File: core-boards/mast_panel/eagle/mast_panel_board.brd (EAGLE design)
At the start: 63.5 x 47.9 mm, 30 parts, among them J1 2-PIN_2MM-V, J4 4-PIN_2MM-H, U1 ATMEGA328P-AUR, U3 MCP2551T-I/SN

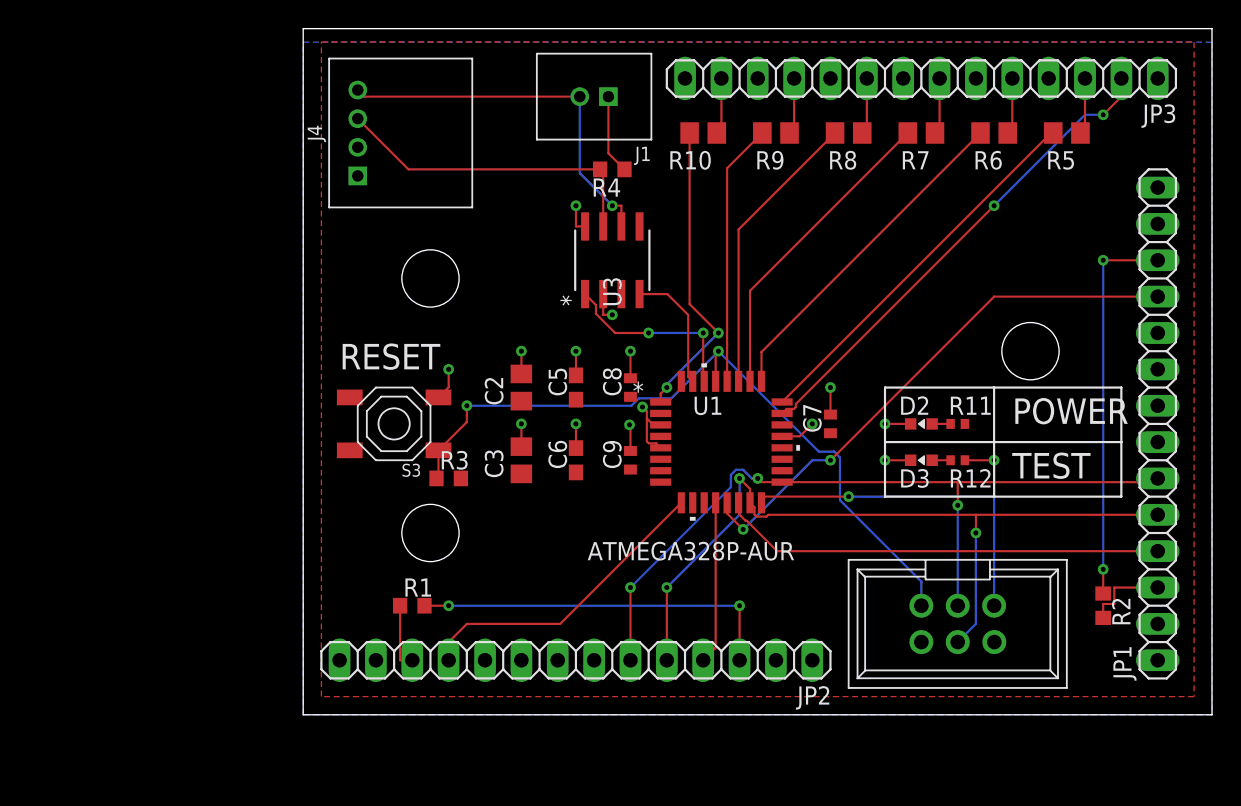
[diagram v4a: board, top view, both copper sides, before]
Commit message: CAN Addition
Added the new CAN Controller. Routing on the board still needs to be done.
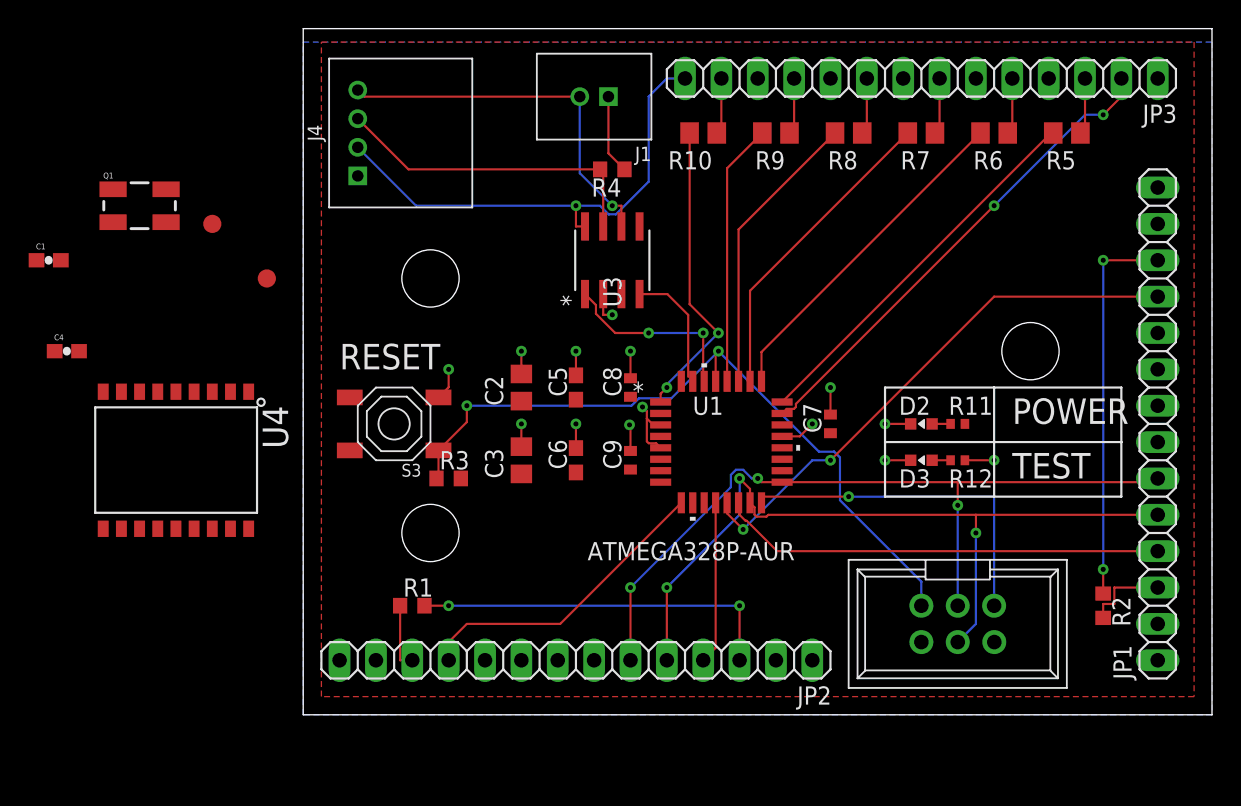
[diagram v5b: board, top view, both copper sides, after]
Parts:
- added C1, C4: 22pF, SparkFun-Capacitors:0603-CAP
- added Q1: 16MHz, SparkFun-FreqCtrl:CRYSTAL-SMD-5X3
- added TP1, TP2: TEST-POINT3X5, SparkFun-Passives:PAD.03X.05
- added U4: MCP2515, SparkFun-DigitalIC:SO-18W
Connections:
- new net CAN_SS: U1.31, U4.16
- new net MBED_CAN_INT: U1.32, U4.12
- new net N$17: C4.2, Q1.3, U4.8
- new net N$18: C1.2, Q1.1, U4.7
- new net VDD: U4.18
- new net VSS: U4.9
- net GND: now also C1.1, C4.1
- net LCD_MOSI: now also U4.14
- net LCD_SCLK: now also U4.13
- net MBED_CAN_RD: now also TP2.P$1, U4.1; no longer U1.30
- net MBED_CAN_TD: now also TP1.P$1, U4.2; no longer U1.31
- net RESET: now also U4.17
- net TEST_LED: now also U4.15
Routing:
- net GND: track 29.5 -> 61.7 mm
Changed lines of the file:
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@@
 <drawing>
 <settings>
-<setting alwaysvectorfont="yes"/>
+<setting alwaysvectorfont="no"/>
 <setting verticaltext="up"/>
 </settings>
@@
 <attribute name="VALUE" x="51.435" y="48.26" size="1.27" layer="27" rot="R180"/>
 </element>
+<element name="U4" library="SparkFun-DigitalIC" package="SO-18W" value="MCP2515" x="13.97" y="22.86" smashed="yes" rot="R180">
+<attribute name="NAME" x="20.0279" y="26.67" size="1.778" layer="25" ratio="10" rot="R270"/>
+<attribute name="PROD_ID" value="IC-09906" x="13.97" y="21.59" size="1.778" layer="27" rot="R180" display="off"/>
+<attribute name="VALUE" x="6.0579" y="26.67" size="1.778" layer="27" ratio="10" rot="R270"/>
+</element>
+<element name="Q1" library="SparkFun-FreqCtrl" package="CRYSTAL-SMD-5X3" value="16MHz" x="11.43" y="40.64" smashed="yes">
+<attribute name="NAME" x="8.89" y="42.545" size="0.4064" layer="25"/>
+<attribute name="PROD_ID" value="XTAL-08218" x="11.43" y="41.91" size="1.778" layer="27" display="off"/>
+<attribute name="VALUE" x="8.89" y="38.1" size="0.4064" layer="27"/>
+</element>
+<element name="C1" library="SparkFun-Capacitors" package="0603-CAP" value="22pF" x="5.08" y="36.83" smashed="yes">
+<attribute name="NAME" x="4.191" y="37.592" size="0.4064" layer="25" font="vector"/>
+<attribute name="PROD_ID" value="CAP-07876" x="-2.54" y="31.75" size="1.778" layer="27" display="off"/>
+<attribute name="VALUE" x="4.064" y="35.687" size="0.4064" layer="27" font="vector"/>
+</element>
+<element name="C4" library="SparkFun-Capacitors" package="0603-CAP" value="22pF" x="6.35" y="30.48" smashed="yes">
+<attribute name="NAME" x="5.461" y="31.242" size="0.4064" layer="25" font="vector"/>
+<attribute name="PROD_ID" value="CAP-07876" x="-5.08" y="21.59" size="1.778" layer="27" display="off"/>
+<attribute name="VALUE" x="5.334" y="29.337" size="0.4064" layer="27" font="vector"/>
+</element>
+<element name="TP1" library="SparkFun-Passives" package="PAD.03X.05" value="TEST-POINT3X5" x="16.51" y="39.37" smashed="yes"/>
+<element name="TP2" library="SparkFun-Passives" package="PAD.03X.05" value="TEST-POINT3X5" x="20.32" y="35.56" smashed="yes"/>
 </elements>
 <signals>
@@
 <wire x1="33.02" y1="27.96" x2="33.02" y2="29.21" width="0.1524" layer="1"/>
 <via x="33.02" y="29.21" extent="1-16" drill="0.35"/>
+<contactref element="C4" pad="1"/>
+<contactref element="C1" pad="1"/>
+<wire x1="26.67" y1="44.72" x2="30.75" y2="40.64" width="0.1524" layer="16"/>
+<wire x1="30.75" y1="40.64" x2="41.91" y2="40.64" width="0.1524" layer="16"/>
+<wire x1="44.19865" y1="40.0332" x2="44.70135" y2="40.0332" width="0.1524" layer="16"/>
+<wire x1="41.91" y1="40.64" x2="43.59185" y2="40.64" width="0.1524" layer="16"/>
+<wire x1="43.59185" y1="40.64" x2="44.19865" y2="40.0332" width="0.1524" layer="16"/>
+<wire x1="44.70135" y1="40.0332" x2="46.99" y2="42.32185" width="0.1524" layer="16"/>
+<wire x1="46.99" y1="42.32185" x2="46.99" y2="48.26" width="0.1524" layer="16"/>
+<wire x1="46.99" y1="48.26" x2="48.26" y2="49.53" width="0.1524" layer="16"/>
+<wire x1="48.26" y1="49.53" x2="49.53" y2="49.53" width="0.1524" layer="16"/>
+<wire x1="74.93" y1="49.53" x2="82.55" y2="41.91" width="0" layer="19" extent="1-1"/>
+<wire x1="69.85" y1="49.53" x2="74.93" y2="49.53" width="0" layer="19" extent="1-1"/>
+<wire x1="64.77" y1="49.53" x2="69.85" y2="49.53" width="0" layer="19" extent="1-1"/>
+<wire x1="59.69" y1="49.53" x2="64.77" y2="49.53" width="0" layer="19" extent="1-1"/>
+<wire x1="54.61" y1="49.53" x2="59.69" y2="49.53" width="0" layer="19" extent="1-1"/>
+<wire x1="49.53" y1="49.53" x2="54.61" y2="49.53" width="0" layer="19" extent="1-1"/>
+<wire x1="43.815" y1="34.4678" x2="42.545" y2="39.1922" width="0" layer="19" extent="1-1"/>
+<wire x1="45.72" y1="30.48" x2="44.45" y2="33.02" width="0" layer="19" extent="1-1"/>
+<wire x1="46.561" y1="26.58061875" x2="45.72" y2="28.59" width="0" layer="19" extent="1-1"/>
+<wire x1="45.65308125" y1="25.33308125" x2="46.561" y2="26.58061875" width="0" layer="19" extent="1-1"/>
+<wire x1="41.91" y1="30.48" x2="44.45" y2="33.02" width="0" layer="19" extent="1-1"/>
+<wire x1="41.91" y1="25.4" x2="41.91" y2="28.79" width="0" layer="19" extent="1-1"/>
+<wire x1="38.1" y1="30.48" x2="41.91" y2="30.48" width="0" layer="19" extent="1-1"/>
+<wire x1="38.1" y1="25.4" x2="38.1" y2="28.89" width="0" layer="19" extent="1-1"/>
+<wire x1="33.02" y1="29.21" x2="38.1" y2="28.89" width="0" layer="19" extent="1-1"/>
+<wire x1="4.23" y1="36.83" x2="26.67" y2="44.72" width="0" layer="19" extent="1-1"/>
+<wire x1="5.5" y1="30.48" x2="4.23" y2="36.83" width="0" layer="19" extent="1-1"/>
+<wire x1="56.3118" y1="24.53" x2="47.8282" y2="25.33" width="0" layer="19" extent="1-1"/>
+<wire x1="59.69" y1="26.05" x2="58.42" y2="25.4" width="0" layer="19" extent="1-1"/>
+<wire x1="63.5" y1="25.4" x2="59.69" y2="26.05" width="0" layer="19" extent="1-1"/>
+<wire x1="65.29" y1="22.86" x2="65.29" y2="25.4" width="0" layer="19" extent="1-1"/>
+<wire x1="66.04" y1="10.16" x2="65.29" y2="22.86" width="0" layer="19" extent="1-1"/>
+<wire x1="58.42" y1="8.89" x2="66.04" y2="10.16" width="0" layer="19" extent="1-1"/>
+<wire x1="82.55" y1="8.89" x2="66.04" y2="10.16" width="0" layer="19" extent="1-1"/>
+<wire x1="25.4" y1="8.89" x2="38.1" y2="23.81" width="0" layer="19" extent="1-1"/>
 </signal>
 <signal name="BUTTON">
@@
 <signal name="MBED_CAN_RD">
 <contactref element="U3" pad="1"/>
-<contactref element="U1" pad="30"/>
-<wire x1="50.87" y1="28.3718" x2="50.8" y2="28.4418" width="0.1524" layer="1"/>
 <wire x1="50.8" y1="28.4418" x2="50.8" y2="31.75" width="0.1524" layer="1"/>
 <via x="50.8" y="31.75" extent="1-16" drill="0.35"/>
@@
 <wire x1="43.307" y1="33.09694375" x2="44.65394375" y2="31.75" width="0.1524" layer="1"/>
 <wire x1="44.65394375" y1="31.75" x2="46.99" y2="31.75" width="0.1524" layer="1"/>
+<contactref element="U4" pad="1"/>
+<contactref element="TP2" pad="P$1"/>
+<wire x1="20.32" y1="35.56" x2="42.545" y2="34.4678" width="0" layer="19" extent="1-1"/>
+<wire x1="19.05" y1="27.6479" x2="20.32" y2="35.56" width="0" layer="19" extent="1-1"/>
 </signal>
 <signal name="MBED_CAN_TD">
 <contactref element="U3" pad="4"/>
-<contactref element="U1" pad="31"/>
 <wire x1="48.2978875" y1="34.4678" x2="46.355" y2="34.4678" width="0.1524" layer="1"/>
 <wire x1="49.7526" y1="33.0130875" x2="48.2978875" y2="34.4678" width="0.1524" layer="1"/>
-<wire x1="50.07" y1="28.3718" x2="49.7526" y2="28.6892" width="0.1524" layer="1"/>
 <wire x1="49.7526" y1="28.6892" x2="49.7526" y2="33.0130875" width="0.1524" layer="1"/>
+<contactref element="U4" pad="2"/>
+<contactref element="TP1" pad="P$1"/>
+<wire x1="17.78" y1="27.6479" x2="46.355" y2="34.4678" width="0" layer="19" extent="1-1"/>
+<wire x1="16.51" y1="39.37" x2="17.78" y2="27.6479" width="0" layer="19" extent="1-1"/>
 </signal>
 <signal name="LCD_SCLK">
@@
 <wire x1="54.19815" y1="21.59" x2="53.59135" y2="22.1968" width="0.1524" layer="16"/>
 <wire x1="45.72" y1="13.97" x2="45.72" y2="8.89" width="0.1524" layer="1"/>
+<contactref element="U4" pad="13"/>
+<wire x1="12.7" y1="18.0721" x2="45.72" y2="13.97" width="0" layer="19" extent="1-1"/>
 </signal>
 <signal name="LCD_MOSI">
@@
 <wire x1="54.5213125" y1="18.923" x2="55.2186875" y2="18.923" width="0.1524" layer="1"/>
 <wire x1="55.2186875" y1="18.923" x2="55.3456875" y2="19.05" width="0.1524" layer="1"/>
+<contactref element="U4" pad="14"/>
+<wire x1="13.97" y1="18.0721" x2="48.26" y2="13.97" width="0" layer="19" extent="1-1"/>
 </signal>
 <signal name="LCD1_SS">
@@
 <wire x1="71.12" y1="12.7" x2="71.12" y2="20.32" width="0.1524" layer="16"/>
 <wire x1="71.12" y1="20.32" x2="71.12" y2="22.86" width="0.1524" layer="16"/>
+<contactref element="U4" pad="15"/>
+<wire x1="15.24" y1="18.0721" x2="54.87" y2="19.8882" width="0" layer="19" extent="1-1"/>
 </signal>
 <signal name="N$1">
@@
 <wire x1="34.29" y1="26.67" x2="34.29" y2="25.53" width="0.1524" layer="1"/>
 <wire x1="34.29" y1="25.53" x2="32.31" y2="23.55" width="0.1524" layer="1"/>
+<contactref element="U4" pad="17"/>
+<wire x1="17.78" y1="18.0721" x2="32.17" y2="21.59" width="0" layer="19" extent="1-1"/>
+</signal>
+<signal name="VDD">
+<contactref element="U4" pad="18"/>
+</signal>
+<signal name="VSS">
+<contactref element="U4" pad="9"/>
+</signal>
+<signal name="N$17">
+<contactref element="Q1" pad="3"/>
+<contactref element="C4" pad="2"/>
+<contactref element="U4" pad="8"/>
+<wire x1="7.2" y1="30.48" x2="13.28" y2="41.79" width="0" layer="19" extent="1-1"/>
+<wire x1="10.16" y1="27.6479" x2="7.2" y2="30.48" width="0" layer="19" extent="1-1"/>
+</signal>
+<signal name="N$18">
+<contactref element="Q1" pad="1"/>
+<contactref element="C1" pad="2"/>
+<contactref element="U4" pad="7"/>
+<wire x1="5.93" y1="36.83" x2="9.58" y2="39.49" width="0" layer="19" extent="1-1"/>
+<wire x1="11.43" y1="27.6479" x2="5.93" y2="36.83" width="0" layer="19" extent="1-1"/>
+</signal>
+<signal name="CAN_SS">
+<contactref element="U4" pad="16"/>
+<contactref element="U1" pad="31"/>
+<wire x1="16.51" y1="18.0721" x2="50.07" y2="28.3718" width="0" layer="19" extent="1-1"/>
+</signal>
+<signal name="MBED_CAN_INT">
+<contactref element="U4" pad="12"/>
+<contactref element="U1" pad="32"/>
+<wire x1="11.43" y1="18.0721" x2="49.27" y2="28.3718" width="0" layer="19" extent="1-1"/>
 </signal>
 </signals>

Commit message: 4/14/20
Added CAN Controller
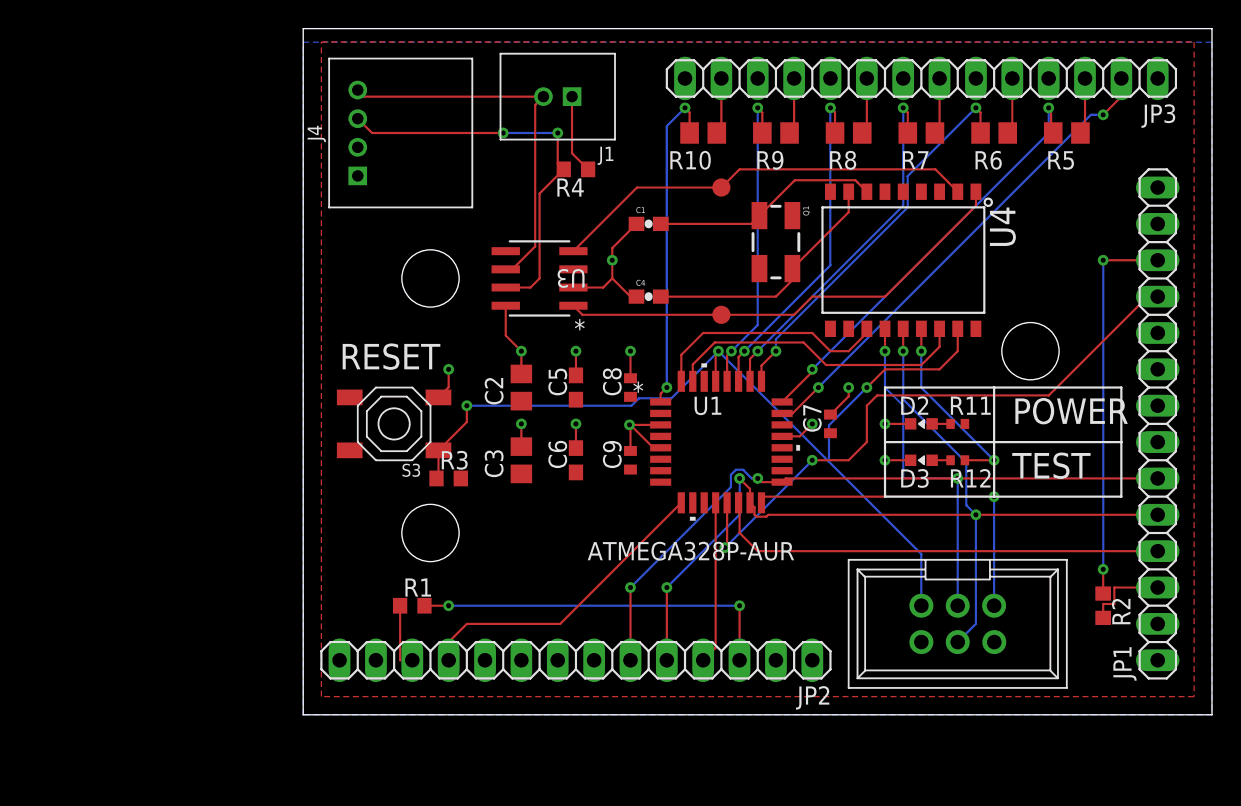
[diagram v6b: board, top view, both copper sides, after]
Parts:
- moved U4 52.7 mm to (64.8, 36.8)
- moved Q1 44.5 mm to (55.9, 38.1), turned to 270 degrees
- moved C1 42.0 mm to (47.0, 39.4)
- moved C4 40.8 mm to (47.0, 34.3)
- moved TP1 35.7 mm to (52.1, 41.9)
- moved TP2 31.9 mm to (52.1, 33.0)
- moved U3 5.24 mm to (39.4, 35.6), turned to 180 degrees
- moved R4 2.54 mm to (41.9, 43.2)
- moved J1 2.54 mm to (40.6, 48.3)
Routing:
- net GND: track 61.7 -> 39.3 mm, vias 14 -> 12
- net MBED_CAN_TD: track 8.32 -> 29.9 mm
- net CAN_SS: track 0.00 -> 21.5 mm
- net MBED_CAN_RD: track 13.0 -> 32.5 mm, vias 2 -> 0
- net N$17: track 0.00 -> 17.5 mm
- net MBED_CAN_INT: track 0.00 -> 16.8 mm
- net N$18: track 0.00 -> 16.0 mm
- net LCD_MOSI: track 55.5 -> 70.6 mm, vias 3 -> 4
- net LCD_SCLK: track 54.9 -> 70.0 mm, vias 3 -> 4
- net RESET: track 51.7 -> 66.3 mm, vias 2 -> 3
- net TEST_LED: track 28.9 -> 40.2 mm, vias 2 -> 3
- net CAN_P: track 22.5 -> 28.0 mm, vias 0 -> 2
- net LCD1_RST: track 38.0 -> 42.2 mm
- net LED_CTRL4: track 20.1 -> 23.7 mm, vias 0 -> 2
- net LED_CTRL5: track 18.4 -> 21.9 mm, vias 0 -> 2
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
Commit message: 4/15/20
Touched up board
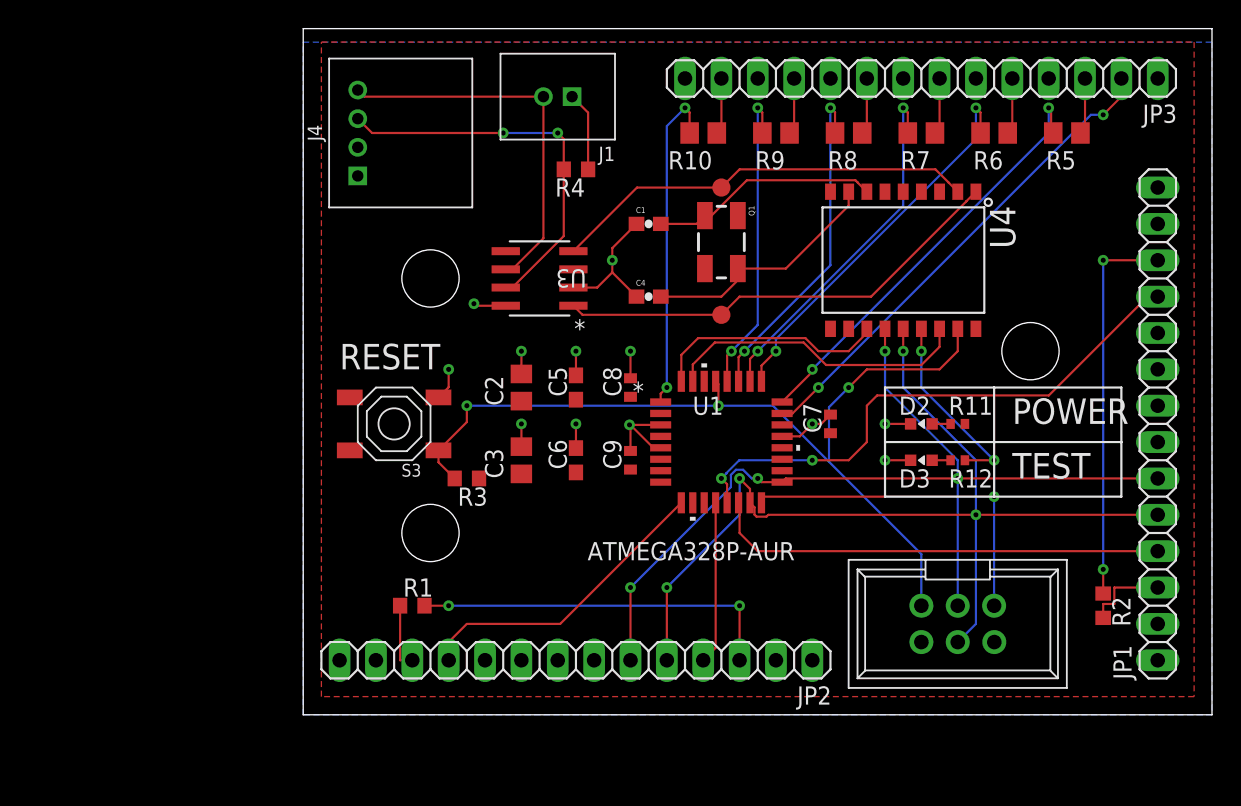
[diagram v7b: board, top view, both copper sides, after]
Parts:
- moved Q1 3.81 mm to (52.1, 38.1)
- moved R3 1.27 mm to (34.3, 21.6)
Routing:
- net LCD1_RST: track 42.2 -> 39.1 mm
- net RESET: track 66.3 -> 63.8 mm
- net GND: track 39.3 -> 37.0 mm
- net LCD_SCLK: track 70.0 -> 67.7 mm
- net CAN_P: track 28.0 -> 27.3 mm
- net MBED_CAN_RD: track 32.5 -> 31.9 mm
